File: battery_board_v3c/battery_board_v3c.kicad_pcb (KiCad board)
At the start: 4 copper layers, 88 x 94.5 mm, 207 parts, among them IC2 PCT2075DP,118, IC3 RP2040_QFN56, IC4 LT3652IMSE#PBF, J1 Bypass, J10 Jetson, J11 BM04B-SRSS-TB(LF)(SN), J12 Z+_Cap_Connector, J14 Solar, J15 FC, J16 I2C Multiplexer Breakout, J17 ISS Foot, J18 Screw_Terminal_01x02, J19 BM04B-SRSS-TB(LF)(SN), J20 CAN1, J21 BM04B-SRSS-TB(LF)(SN), J22 CAN2, J23 Conn_ARM_JTAG_SWD_10, J24 USB_B_Micro, J25 Life Makes Lemonade, J26 BM04B-SRSS-TB(LF)(SN), J27 I2C0 Breakout, J3 Heater, J5 Foot0, J6 Foot1, J7 Foot2, J8 Foot3, J9 RBF, K1 APAN3105, Q1 IRF7458, Q10 IRLML2803, Q11 NDS8434, Q2 IRF7458, Q3 MBT2222ADW1T1, Q4 MMBT2222AT, Q5 MBT2222ADW1T1, Q6 IRLML2803, Q7 IRLML2803, Q8 NDS8434, Q9 NDS8434, SW1 KMR2, SW2 KMR2, U1 R5460N208AA, U10 TLVH431 DBZ SOT-23, U11 MCP25625-E/ML, U12 INA219AxD, U13 MAX706RESA, U14 INA219AxD, U2 1049, U3 TPS54226PWPRPWP14_2P31X2P46-L, U4 1049, U5 TPS54226PWPRPWP14_2P31X2P46-L, U6 TPS7A4501DCQT, U7 ADS1015IDGS, U8 W25Q128JV, U9 AD8495, Y1 Crystal_GND24, Y2 Crystal_GND24

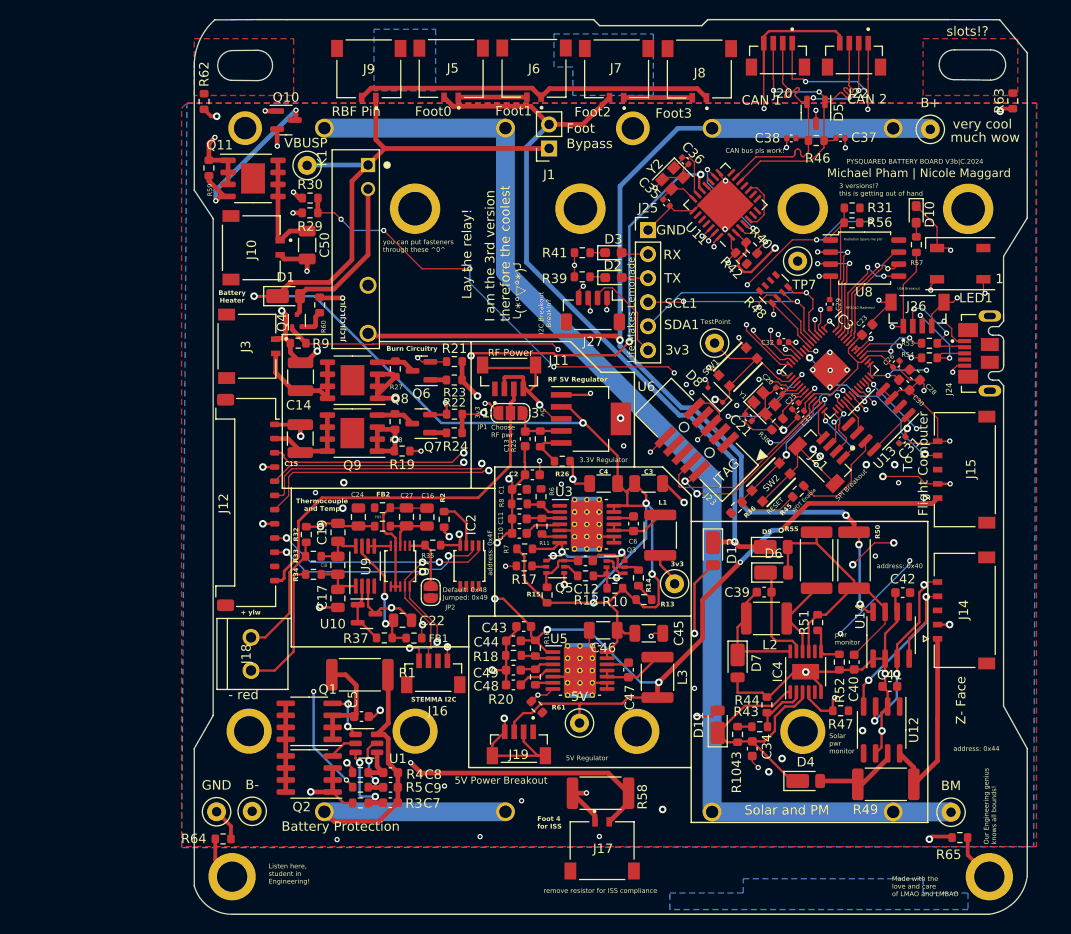
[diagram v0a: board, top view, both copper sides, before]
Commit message: Finished Temperature Sensor layouts
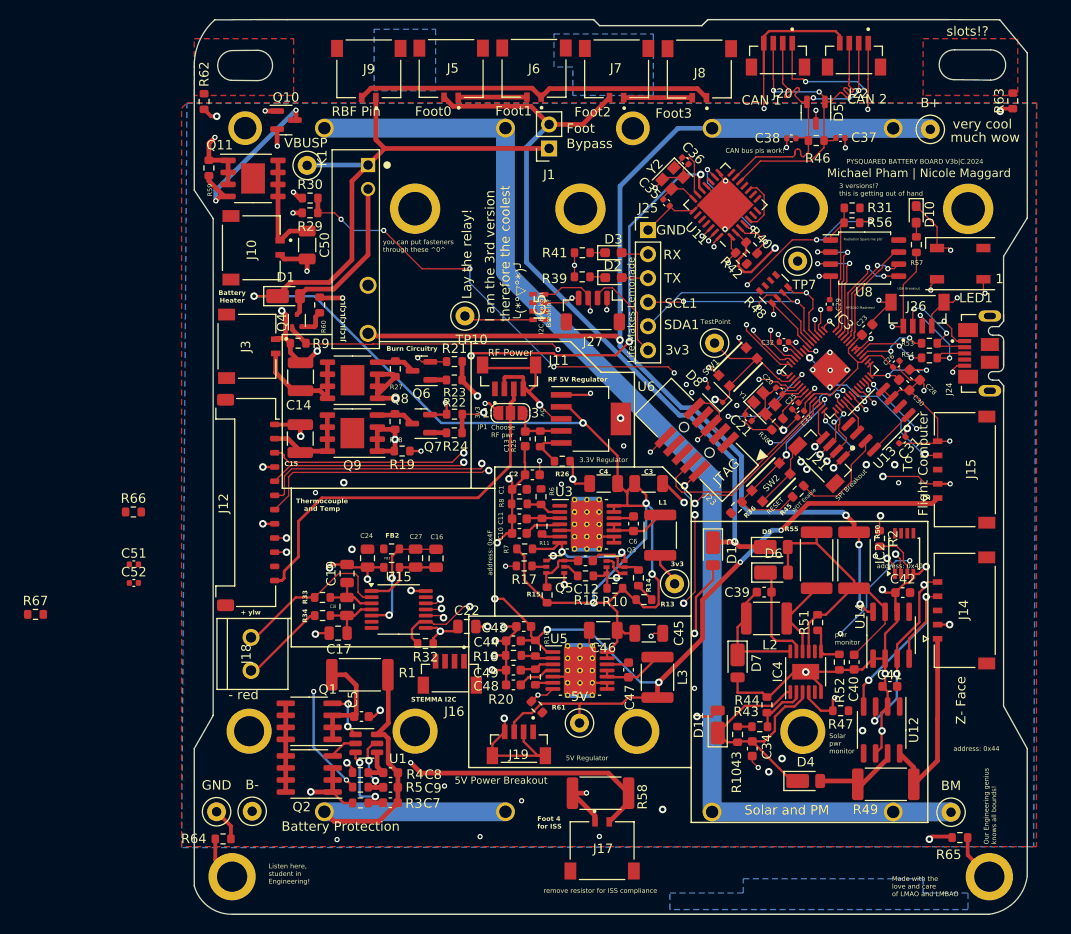
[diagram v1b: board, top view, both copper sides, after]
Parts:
- removed FB1: FerriteBead, Resistor_SMD:R_0603_1608Metric
- removed JP2: SolderJumper_2_Open, Jumper:SolderJumper-2_P1.3mm_Open_RoundedPad1.0x1.5mm
- removed R35: 10k-Ohm, Resistor_SMD:R_0603_1608Metric
- removed R37: 1k, Resistor_SMD:R_0603_1608Metric
- removed U10: TLVH431 DBZ SOT-23, Package_TO_SOT_SMD:SOT-23
- removed U7: ADS1015IDGS, Package_SO:TSSOP-10_3x3mm_P0.5mm
- removed U9: AD8495, Package_SO:MSOP-8_3x3mm_P0.65mm
- added C51: 100nf, Capacitor_SMD:C_0402_1005Metric, F.Cu at (104.1, 98.5)
- added C52: 100nf, Capacitor_SMD:C_0402_1005Metric, F.Cu at (104.1, 100.5)
- added IC5: RV-3028-C7_32.768kHz_1ppm_TA_QC, RTC:RV3028C7, F.Cu at (146.9, 71.3)
- added R66: 10k, Resistor_SMD:R_0603_1608Metric, F.Cu at (104.1, 93.0)
- added R67: 10k, Resistor_SMD:R_0603_1608Metric, F.Cu at (93.7, 103.8)
- added TP10: RESET, TestPoint:TestPoint_Loop_D1.80mm_Drill1.0mm_Beaded, F.Cu at (139.1, 72.3)
- added U15: MAX31856, Package_SO:TSSOP-14_4.4x5mm_P0.65mm, F.Cu at (132.1, 103.3)
- C16: value 10uF -> 0.1uF
- C22: value 1uF -> 0.1uF
- R32: value 1-MOhm -> 10k
- moved R2 46.0 mm to (182.9, 95.8), turned to -90 degrees
- moved IC2 45.9 mm to (185.5, 97.4), turned to 90 degrees
- moved R32 17.1 mm to (134.9, 106.9), turned to 180 degrees
- moved C22 6.83 mm to (139.3, 105.1)
- moved FB2 4.46 mm to (131.3, 96.9)
- moved C18 4.46 mm to (126.6, 103.0)
- moved C27 4.46 mm to (133.9, 97.9)
- moved C16 4.46 mm to (136.0, 97.9)
- moved C19 4.46 mm to (126.6, 99.5)
- moved C24 4.46 mm to (128.8, 97.9)
- moved FB3 4.46 mm to (131.4, 98.9)
- moved R33 4.46 mm to (124.1, 103.9)
- moved R34 4.46 mm to (124.0, 102.0)
- moved C17 3.67 mm to (125.7, 105.8), turned to 0 degrees
- moved J16 1.75 mm to (137.5, 111.3)
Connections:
- C22 pad 1: Net-(U9-+Vs) -> +3V3
- R32 pad 1: Net-(J18-Pin_2) -> +3V3
- R32 pad 2: GND -> SPI1_CS0
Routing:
- net SCL0: track 164.3 -> 75.1 mm, vias 10 -> 5
- net SDA0: track 158.4 -> 73.3 mm, vias 7 -> 6
- net SPI1_CS0: track 6.66 -> 67.1 mm, vias 2 -> 6
- net SPI1_SCK: track 5.30 -> 61.3 mm, vias 0 -> 2
- net SPI1_MOSI: track 5.08 -> 60.4 mm, vias 2 -> 4
- net SPI1_MISO: track 3.52 -> 58.1 mm, vias 0 -> 2
- net Net-(U9-+Vs): track 13.6 -> 0.00 mm, vias 2 -> 0
- net Net-(IC5-EVI): track 0.00 -> 7.37 mm
- net Net-(U10-K): track 6.71 -> 0.00 mm
- net Net-(JP2-A): track 6.21 -> 0.00 mm
- net GND: track 319.9 -> 313.9 mm, vias 65 -> 69
- net SDA1: track 34.2 -> 39.7 mm
- net Net-(J18-Pin_1): track 15.1 -> 9.51 mm
- net +3V3: track 68.3 -> 72.6 mm
- net Net-(J18-Pin_2): track 13.9 -> 17.8 mm
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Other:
- board text removed: "Default: 0x48 Jumped: 0x49"

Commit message: Finished RTC Layout
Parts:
- added C53: 1uF, Capacitor_SMD:C_0603_1608Metric, F.Cu at (148.2, 68.2)
- moved R67 60.2 mm to (144.7, 71.8), turned to 90 degrees
- moved C52 51.3 mm to (144.8, 69.3), turned to 90 degrees
- moved C51 49.2 mm to (143.7, 69.3), turned to 90 degrees
- moved R66 43.5 mm to (142.5, 72.7), turned to 90 degrees
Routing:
- net V_BACKUP: track 0.00 -> 17.5 mm, vias 0 -> 2
- net GND: track 313.9 -> 322.8 mm, vias 69 -> 71
- net RTC_INT: track 0.00 -> 8.28 mm
- net +3V3: track 72.6 -> 77.0 mm, vias 29 -> 30

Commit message: Cleaned Up Design Rule Errors
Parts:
- moved J16 56.9 mm to (194.3, 114.7), turned to -90 degrees
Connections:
- J12 pad 10: SCL0 -> SCL1
- J12 pad 9: SDA0 -> SDA1
- J15 pad 1: +5V -> V_RF
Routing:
- net SDA1: track 39.7 -> 91.2 mm, vias 2 -> 3
- net SCL1: track 34.6 -> 84.2 mm, vias 3 -> 4
- net V_RF: track 41.8 -> 90.1 mm, vias 0 -> 2
- net +5V: track 156.9 -> 117.0 mm, vias 8 -> 6
- net SDA0: track 73.3 -> 89.6 mm, vias 6 -> 5
- net SCL0: track 75.1 -> 91.2 mm, vias 5 -> 4
- net GND: track 322.8 -> 333.3 mm, vias 71 -> 74
- net ENAB_BURN: track 43.4 -> 47.0 mm
- net +3V3: track 77.0 -> 78.8 mm, vias 30 -> 36
- net PACK+: track 213.1 -> 212.3 mm

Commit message: V3c as Ordered July 16 2024
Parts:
- removed C15: 200uF, Capacitor_SMD:C_1210_3225Metric
- removed R45: 10k, Resistor_SMD:R_0603_1608Metric
- added C54: 100uF, Capacitor_SMD:C_1206_3216Metric, F.Cu at (121.8, 78.7)
- added JP2: WDT_Enable, Jumper:SolderJumper-2_P1.3mm_Open_TrianglePad1.0x1.5mm, F.Cu at (174.4, 92.5)
- added JP3: NEO_PWR Enable, Jumper:SolderJumper-2_P1.3mm_Open_TrianglePad1.0x1.5mm, F.Cu at (194.6, 67.5)
- added R35: 10k, Resistor_SMD:R_0603_1608Metric, F.Cu at (162.5, 64.5)
- C14: value 200uF -> 100uF; footprint Capacitor_SMD:C_1210_3225Metric -> Capacitor_SMD:C_1206_3216Metric
- moved C14 6.27 mm to (122.0, 85.0)
- moved C41 3.96 mm to (187.8, 112.5), turned to 90 degrees
- moved R57 3.16 mm to (186.8, 61.6)
- moved D10 2.58 mm to (184.3, 60.8), turned to 0 degrees
- moved D4 2.36 mm to (177.4, 120.8)
- moved LED1 1.62 mm to (189.8, 66.8)
- moved U12 1.50 mm to (184.1, 114.9)
- moved R49 1.12 mm to (183.9, 120.7)
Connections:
- net /A0 renamed SPI1_CS1
- C14 pad 1: Heater -> BURN
- IC3 pad 37: /NEO_PWR -> CAN_INT
- IC3 pad 39: /A1 -> RTC_INT
- U11 pad 25: unconnected-(U11-INT-Pad25) -> CAN_INT
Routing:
- net RTC_INT: track 8.28 -> 49.5 mm, vias 0 -> 2
- net CAN_INT: track 0.00 -> 31.4 mm, vias 0 -> 2
- net /NEO_PWR: track 21.0 -> 2.44 mm, vias 2 -> 0
- net +3V3: track 78.8 -> 96.4 mm, vias 36 -> 41
- net GND: track 333.3 -> 326.5 mm, vias 74 -> 76
- net SCL0: track 91.2 -> 84.6 mm, vias 4 -> 5
- net SDA0: track 89.6 -> 84.9 mm, vias 5 -> 3
- net VSOLAR: track 20.3 -> 16.4 mm
- net VBUS: track 18.8 -> 22.0 mm
- net Net-(D11-K): track 28.2 -> 30.3 mm
- net Net-(U11-RESET): track 12.5 -> 14.0 mm
- net VSOLAR_I: track 8.95 -> 7.54 mm
- net FC_RESET: track 19.6 -> 20.1 mm
- net ENAB_RF: track 25.3 -> 25.4 mm, vias 3 -> 2
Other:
- board text added: "IT'S FREE REAL ESTATE"
- board text added: "PYSQUARED BATTERY BOARD V3c|C.2024"
- board text added: "This land could be yours for the low low price of $100k"
- board text removed: "PYSQUARED BATTERY BOARD V3b|C.2024"
- board text removed: "address: 0x4F"
